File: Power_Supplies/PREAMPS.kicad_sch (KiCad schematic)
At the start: 142 parts, among them J10 XLR3_AudioJack3_Combo, J20 ACJM-MV-2, J3 XLR3_AudioJack3_Combo, J4 XLR3_AudioJack3_Combo, J5 ACJM-MV-2, J6 ACJM-MV-2, J7 ACJM-MV-2, J9 XLR3_AudioJack3_Combo, SW1 SW_Push, SW2 SW_Push, SW3 SW_Push, SW4 SW_Push, U15 OPA2134, U16 SSM2019BRNZ, U17 SSM2019BRNZ, U18 OPA2134, U19 SSM2019BRNZ, U20 SSM2019BRNZ

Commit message: Added stuff for the power supply circuitry
changed all grounds to GND (same ground plane)
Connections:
- net AGND: no longer C106.2, C107.2, C108.2, C109.2, C54.1, C55.1, C56.1, C57.1, C60.1, C61.1, C62.1, C63.1, C64.2, C67.2, C76.1, C77.1, C78.2, C79.2, C82.2, C83.2, C84.1, C85.1, C86.1, C87.1, C88.1, C89.1, C90.1, C91.1, C92.1, C93.1, C94.2, C97.2, DZ10.2 (A), DZ12.2 (A), DZ14.2 (A), DZ16.2 (A), DZ2.2 (A), DZ4.2 (A), DZ6.2 (A), DZ8.2 (A), J10.S, J20.1, J3.S, J4.S, J5.1, J6.1, J7.1, J9.S, R42.2, R43.2, R48.1, R49.1, R55.2, R57.2, R62.1, R63.1, R66.1, R67.1, R68.2, R69.2, R72.2, R73.2, R84.1, R86.1, U16.5 (REFERENCE), U17.5 (REFERENCE), U19.5 (REFERENCE), U20.5 (REFERENCE)
- new net GND: C106.2, C107.2, C108.2, C109.2, C54.1, C55.1, C56.1, C57.1, C60.1, C61.1, C62.1, C63.1, C64.2, C67.2, C76.1, C77.1, C78.2, C79.2, C82.2, C83.2, C84.1, C85.1, C86.1, C87.1, C88.1, C89.1, C90.1, C91.1, C92.1, C93.1, C94.2, C97.2, DZ10.2 (A), DZ12.2 (A), DZ14.2 (A), DZ16.2 (A), DZ2.2 (A), DZ4.2 (A), DZ6.2 (A), DZ8.2 (A), J10.S, J20.1, J3.S, J4.S, J5.1, J6.1, J7.1, J9.S, R42.2, R43.2, R48.1, R49.1, R55.2, R57.2, R62.1, R63.1, R66.1, R67.1, R68.2, R69.2, R72.2, R73.2, R84.1, R86.1, U16.5 (REFERENCE), U17.5 (REFERENCE), U19.5 (REFERENCE), U20.5 (REFERENCE)

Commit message: Add files via upload
fixed voltage issues
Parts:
- removed D1, D2, D3, D4: LED, LED_SMD:LED_0201_0603Metric, symbol PCM_SL_Devices:LED
- removed R42, R43, R72, R73: 2.2k, Resistor_SMD:R_0805_2012Metric, symbol Device:R
- removed SW1, SW2, SW3, SW4: SW_Push, Button_Switch_THT:SW_PUSH_1P1T_6x3.5mm_H5.0_APEM_MJTP1250, symbol Switch:SW_Push
- added J28, J29, J30, J31: PINHD_1x2_Male, Connector_PinHeader_2.54mm:PinHeader_1x02_P2.54mm_Vertical, symbol PCM_SL_Pin_Headers:PINHD_1x2_Male
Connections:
- net -5V_1 is gone; now on net -12V: C85.2, U18.4 (V-)
- net 36V: now also J28.1, J29.1, J30.1, J31.1
- net AGND: no longer J10.1, J3.1, J4.1, J9.1, R60.1, R61.1
- net GND: now also J10.1, J3.1, J4.1, J9.1, R60.1, R61.1
- net at R56.2: now also J29.2
- net at R83.2: now also J31.2
- net at R54.2: now also J28.2
- net at R82.2: now also J30.2
- net -5V renamed -12V
- net 5V renamed 12V

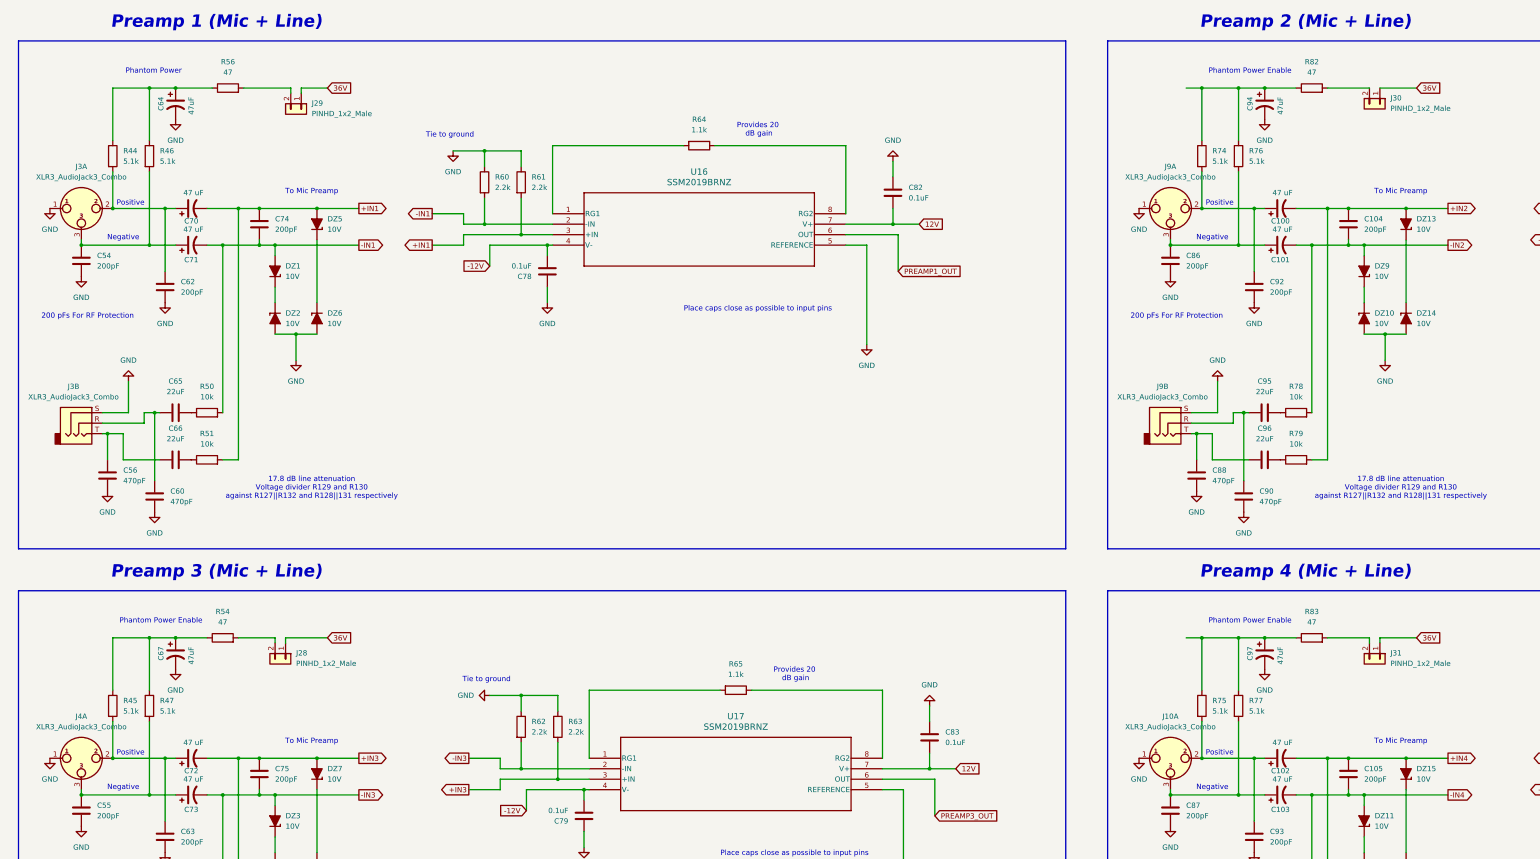
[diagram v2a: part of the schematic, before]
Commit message: connected ADC/DACs, USB
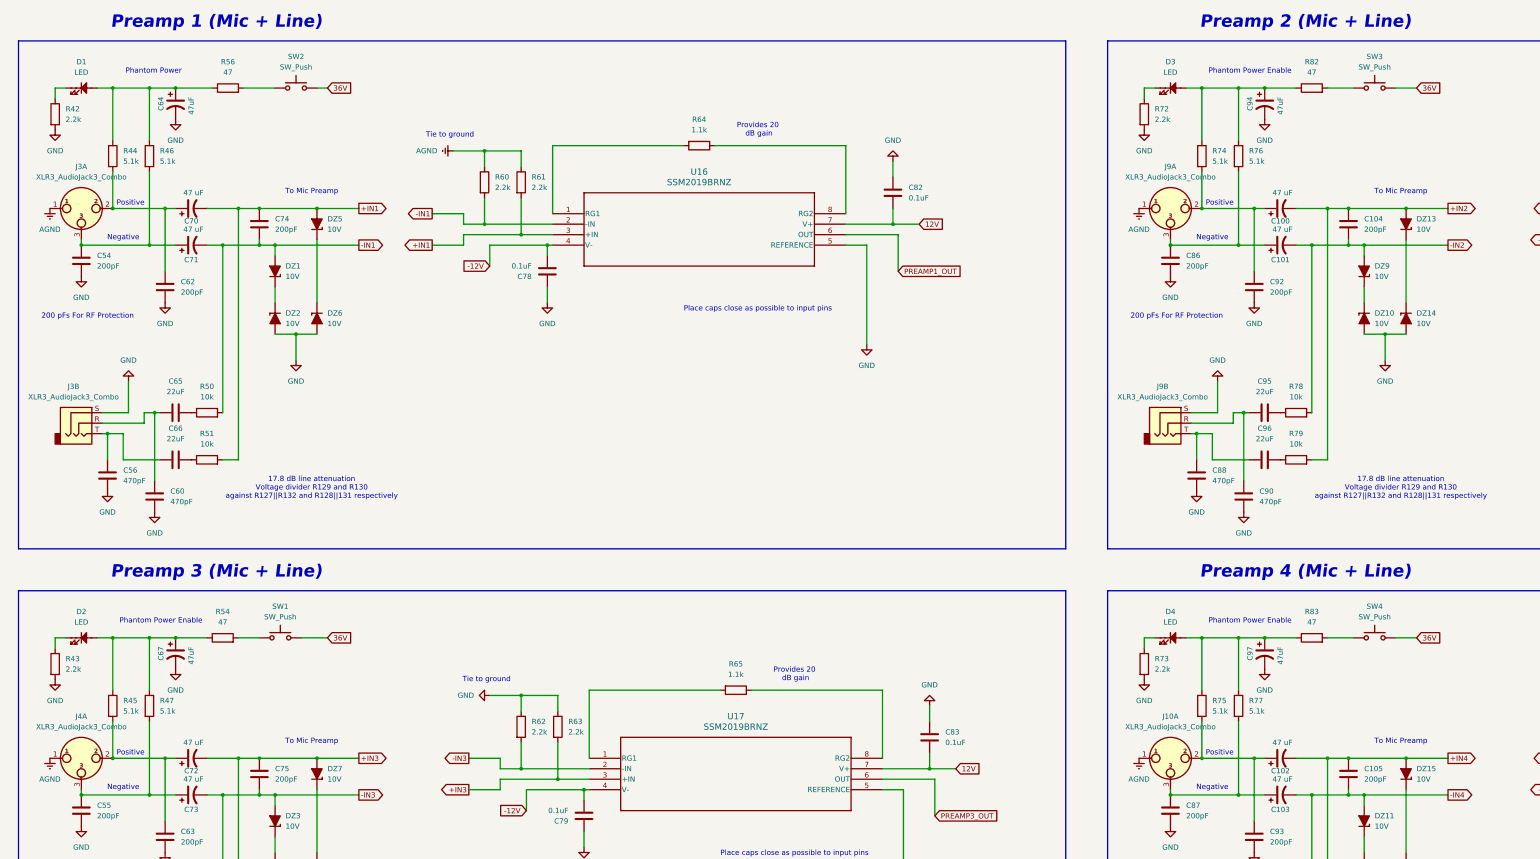
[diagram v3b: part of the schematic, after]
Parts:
- removed J28, J29, J30, J31: PINHD_1x2_Male, Connector_PinHeader_2.54mm:PinHeader_1x02_P2.54mm_Vertical, symbol PCM_SL_Pin_Headers:PINHD_1x2_Male
- added D1, D2, D3, D4: LED, LED_SMD:LED_0201_0603Metric, symbol PCM_SL_Devices:LED
- added R42, R43, R72, R73: 2.2k, Resistor_SMD:R_0805_2012Metric, symbol Device:R
- added SW1, SW2, SW3, SW4: SW_Push, Button_Switch_THT:SW_PUSH_1P1T_6x3.5mm_H5.0_APEM_MJTP1250, symbol Switch:SW_Push
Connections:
- net 36V: now also SW1.2, SW2.2, SW3.2, SW4.2
- net AGND: now also J10.1, J3.1, J4.1, J9.1, R60.1, R61.1
- net GND: now also R42.2, R43.2, R72.2, R73.2; no longer J10.1, J3.1, J4.1, J9.1, R60.1, R61.1
- net at C97.1, R75.1, R77.1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: now also D4.2
- net at C67.1, R45.1, R47.1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: now also D2.2
- net at R54.2: now also SW1.1
- net at C64.1, R44.1, R46.1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: now also D1.2
- net at R56.2: now also SW2.1
- net at R83.2: now also SW4.1
- net at C94.1, R74.1, R76.1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: now also D3.2
- net at R82.2: now also SW3.1
- new net: D4.1, R73.1
- new net: D3.1, R72.1
- new net: D1.1, R42.1
- new net: D2.1, R43.1

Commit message: Add files via upload
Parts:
- removed D1, D2, D3, D4: LED, LED_SMD:LED_0201_0603Metric, symbol PCM_SL_Devices:LED
- removed R42, R43, R72, R73: 2.2k, Resistor_SMD:R_0805_2012Metric, symbol Device:R
- removed SW1, SW2, SW3, SW4: SW_Push, Button_Switch_THT:SW_PUSH_1P1T_6x3.5mm_H5.0_APEM_MJTP1250, symbol Switch:SW_Push
- added J29, J30, J31, J32: PINHD_1x2_Female, Connector_PinSocket_2.54mm:PinSocket_1x02_P2.54mm_Vertical, symbol PCM_SL_Pin_Headers:PINHD_1x2_Female
- J10, J3, J4, J9: footprint Connector_Audio:Jack_XLR-6.35mm_Neutrik_NCJ5FI-H-0_Horizontal -> Connector_Audio:Jack_XLR-6.35mm_Neutrik_NCJ6FA-H_Horizontal
- J20, J5, J6, J7: footprint ACJMMV2 -> SamacSys_Parts:ACJMMV2
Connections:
- net AGND is gone; now on net GND: J10.1, J3.1, J4.1, J9.1, R60.1, R61.1, R85.1, R87.1
- net 36V: now also J29.1, J30.1, J31.1, J32.1
- net at R56.2: now also J30.2
- net at R83.2: now also J32.2
- net at R54.2: now also J29.2
- net at R82.2: now also J31.2
- net INST1_OUT renamed AIN_6
- net INST2_OUT renamed AIN_5
- net INST3_OUT renamed AIN_8
- net INST4_OUT renamed AIN_7
- net PREAMP1_OUT renamed AIN_1
- net PREAMP2_OUT renamed AIN_2
- net PREAMP3_OUT renamed AIN_3
- net PREAMP4_OUT renamed AIN_4
